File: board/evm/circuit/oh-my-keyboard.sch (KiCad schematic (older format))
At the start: 0 parts

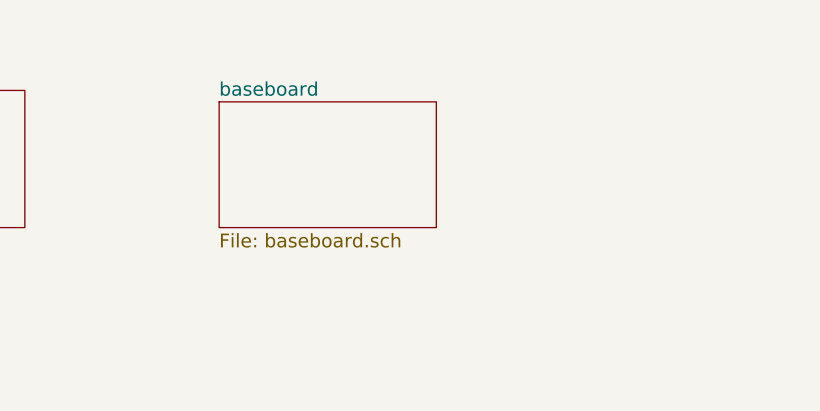
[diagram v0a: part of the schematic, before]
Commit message: add cpld
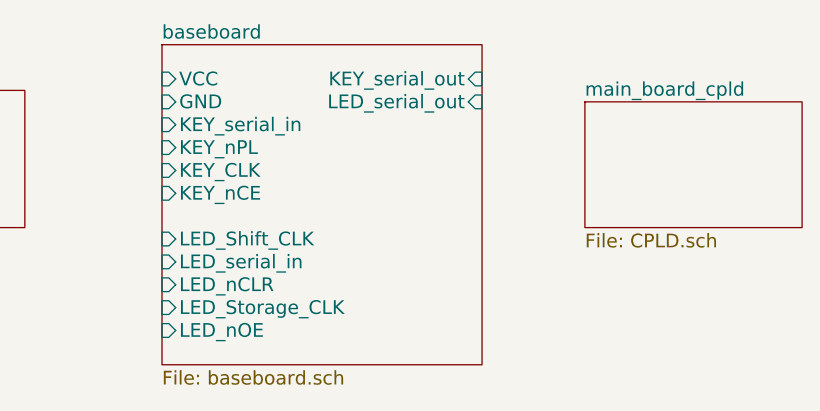
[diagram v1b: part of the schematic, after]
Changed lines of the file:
@@
 LIBS:stm8
 LIBS:stm32
+LIBS:74xgxx
+LIBS:ac-dc
+LIBS:actel
+LIBS:Altera
+LIBS:analog_devices
+LIBS:battery_management
+LIBS:bbd
+LIBS:brooktre
+LIBS:cmos_ieee
+LIBS:dc-dc
+LIBS:diode
+LIBS:elec-unifil
+LIBS:ESD_Protection
+LIBS:ftdi
+LIBS:gennum
+LIBS:graphic
+LIBS:hc11
+LIBS:ir
+LIBS:Lattice
+LIBS:logo
+LIBS:maxim
+LIBS:microchip_dspic33dsc
+LIBS:microchip_pic10mcu
+LIBS:microchip_pic12mcu
+LIBS:microchip_pic16mcu
+LIBS:microchip_pic18mcu
+LIBS:microchip_pic32mcu
+LIBS:motor_drivers
+LIBS:msp430
+LIBS:nordicsemi
+LIBS:nxp_armmcu
+LIBS:onsemi
+LIBS:Oscillators
+LIBS:powerint
+LIBS:Power_Management
+LIBS:pspice
+LIBS:references
+LIBS:relays
+LIBS:rfcom
+LIBS:sensors
+LIBS:silabs
+LIBS:supertex
+LIBS:switches
+LIBS:transf
+LIBS:ttl_ieee
+LIBS:video
+LIBS:Worldsemi
+LIBS:Xicor
+LIBS:Zilog
+LIBS:my_kicad
 LIBS:oh-my-keyboard-cache
 EELAYER 25 0
@@
 $Descr A2 23386 16535
 encoding utf-8
-Sheet 1 3
+Sheet 1 4
 Title ""
 Date ""
@@
 $EndSheet
 $Sheet
-S 3800 1700 950  550
+S 3550 1450 1400 1400
 U 57532E7E
 F0 "baseboard" 60
 F1 "baseboard.sch" 60
+F2 "VCC" I L 3550 1600 60
+F3 "GND" I L 3550 1700 60
+F4 "KEY_serial_in" I L 3550 1800 60
+F5 "KEY_nPL" I L 3550 1900 60
+F6 "KEY_CLK" I L 3550 2000 60
+F7 "KEY_nCE" I L 3550 2100 60
+F8 "KEY_serial_out" I R 4950 1600 60
+F9 "LED_Shift_CLK" I L 3550 2300 60
+F10 "LED_serial_in" I L 3550 2400 60
+F11 "LED_nCLR" I L 3550 2500 60
+F12 "LED_Storage_CLK" I L 3550 2600 60
+F13 "LED_nOE" I L 3550 2700 60
+F14 "LED_serial_out" I R 4950 1700 60
+$EndSheet
+$Sheet
+S 5400 1700 950  550
+U 5755DB2C
+F0 "main_board_cpld" 60
+F1 "CPLD.sch" 60
 $EndSheet
 $EndSCHEMATC

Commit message: add lots of ICs
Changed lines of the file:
@@
 $Descr A2 23386 16535
 encoding utf-8
-Sheet 1 4
+Sheet 1 8
 Title ""
 Date ""
@@
 F1 "CPLD.sch" 60
 $EndSheet
+$Sheet
+S 2100 3300 1400 950
+U 57545D59
+F0 "nRF24L01" 60
+F1 "nrf24l01.sch" 60
+$EndSheet
+$Sheet
+S 4100 3300 2050 1000
+U 57545D83
+F0 "BlueTooth" 60
+F1 "bluetooth.sch" 60
+$EndSheet
+$Sheet
+S 2150 4750 1400 900
+U 5754760F
+F0 "UsbDongle" 60
+F1 "usb_dongle.sch" 60
+$EndSheet
+$Sheet
+S 4150 4750 1700 850
+U 57549417
+F0 "Touch" 60
+F1 "touch.sch" 60
+$EndSheet
 $EndSCHEMATC

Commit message: basic works for mcu
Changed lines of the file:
@@
 LIBS:contrib
 LIBS:valves
-LIBS:stm8
-LIBS:stm32
-LIBS:74xgxx
-LIBS:ac-dc
-LIBS:actel
 LIBS:Altera
-LIBS:analog_devices
-LIBS:battery_management
-LIBS:bbd
-LIBS:brooktre
-LIBS:cmos_ieee
-LIBS:dc-dc
-LIBS:diode
-LIBS:elec-unifil
-LIBS:ESD_Protection
-LIBS:ftdi
-LIBS:gennum
-LIBS:graphic
-LIBS:hc11
-LIBS:ir
-LIBS:Lattice
-LIBS:logo
-LIBS:maxim
-LIBS:microchip_dspic33dsc
-LIBS:microchip_pic10mcu
-LIBS:microchip_pic12mcu
-LIBS:microchip_pic16mcu
-LIBS:microchip_pic18mcu
-LIBS:microchip_pic32mcu
-LIBS:motor_drivers
-LIBS:msp430
-LIBS:nordicsemi
-LIBS:nxp_armmcu
-LIBS:onsemi
-LIBS:Oscillators
-LIBS:powerint
-LIBS:Power_Management
-LIBS:pspice
-LIBS:references
-LIBS:relays
-LIBS:rfcom
-LIBS:sensors
-LIBS:silabs
-LIBS:supertex
-LIBS:switches
-LIBS:transf
-LIBS:ttl_ieee
-LIBS:video
-LIBS:Worldsemi
-LIBS:Xicor
-LIBS:Zilog
 LIBS:my_kicad
 LIBS:oh-my-keyboard-cache
@@
 F0 "MCU" 60
 F1 "mcu.sch" 60
+F2 "VCC" I L 2050 1750 60
+F3 "GND" I L 2050 1900 60
+F4 "VCC_5V" I L 2050 2050 60
 $EndSheet
 $Sheet

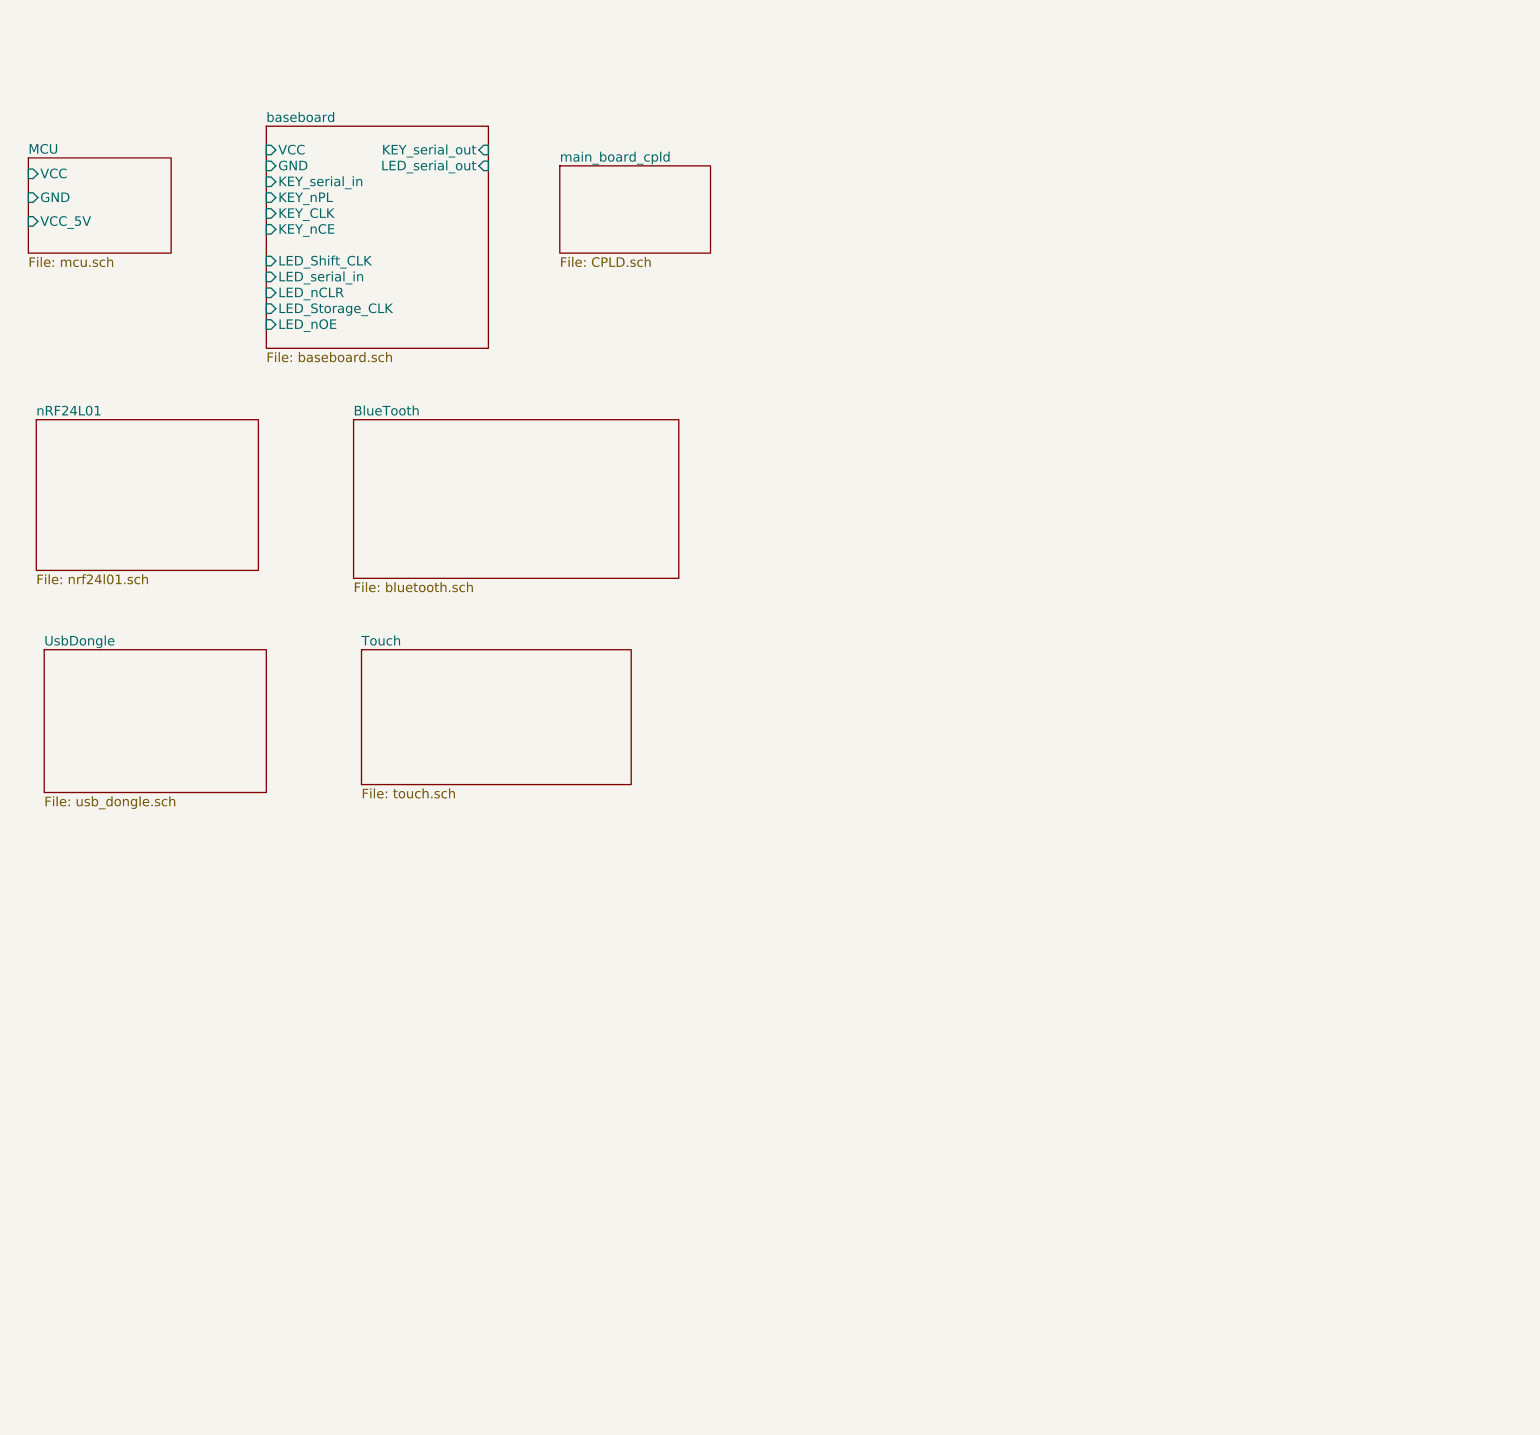
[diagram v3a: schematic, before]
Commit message: add more schs
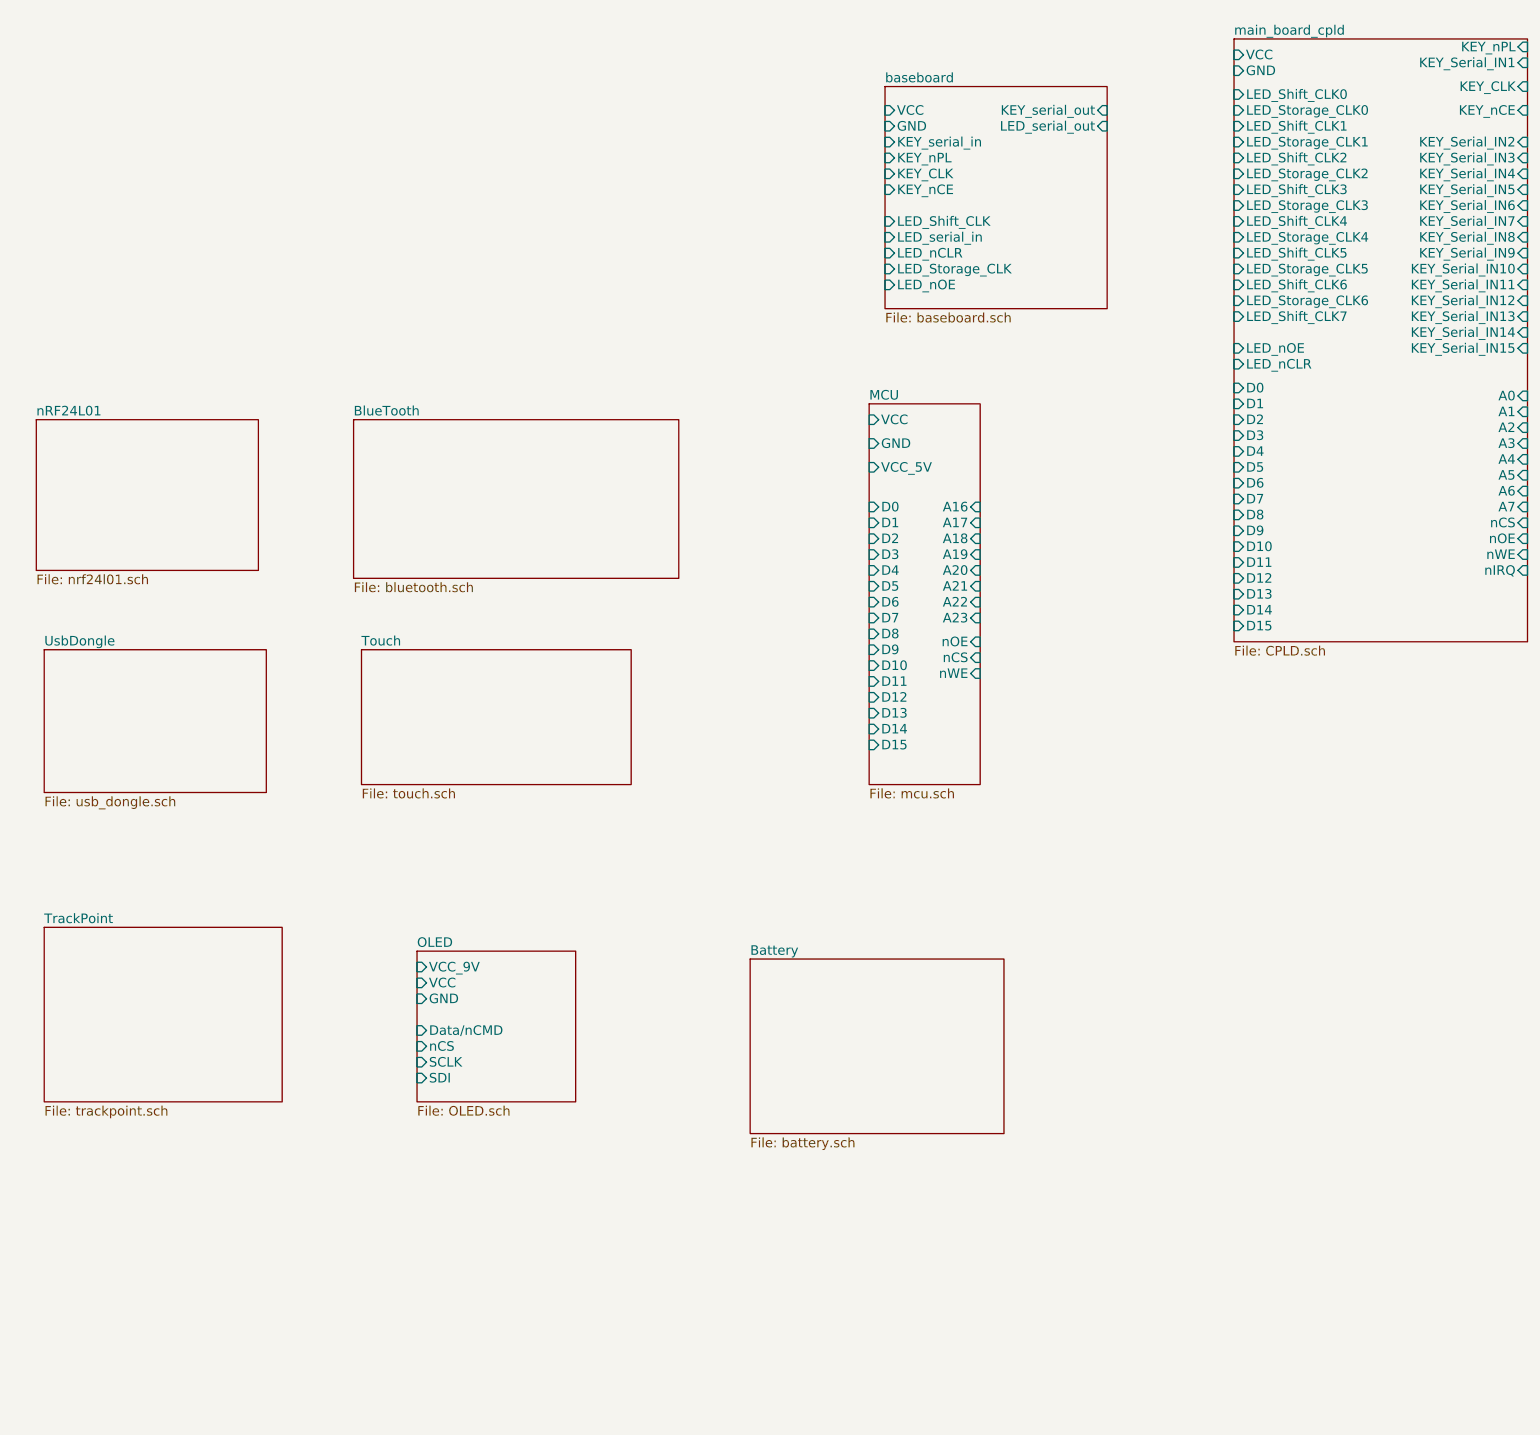
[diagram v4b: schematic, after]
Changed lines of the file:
@@
 LIBS:contrib
 LIBS:valves
+LIBS:stm8
+LIBS:stm32
+LIBS:74xgxx
+LIBS:ac-dc
+LIBS:actel
 LIBS:Altera
+LIBS:analog_devices
+LIBS:battery_management
+LIBS:bbd
+LIBS:brooktre
+LIBS:cmos_ieee
+LIBS:dc-dc
+LIBS:diode
+LIBS:elec-unifil
+LIBS:ESD_Protection
+LIBS:ftdi
+LIBS:gennum
+LIBS:graphic
+LIBS:hc11
+LIBS:ir
+LIBS:Lattice
+LIBS:logo
+LIBS:maxim
+LIBS:microchip_dspic33dsc
+LIBS:microchip_pic10mcu
+LIBS:microchip_pic12mcu
+LIBS:microchip_pic16mcu
+LIBS:microchip_pic18mcu
+LIBS:microchip_pic32mcu
+LIBS:motor_drivers
+LIBS:msp430
+LIBS:nordicsemi
+LIBS:nxp_armmcu
+LIBS:onsemi
+LIBS:Oscillators
+LIBS:powerint
+LIBS:Power_Management
+LIBS:pspice
+LIBS:references
+LIBS:relays
+LIBS:rfcom
+LIBS:sensors
+LIBS:silabs
+LIBS:supertex
+LIBS:switches
+LIBS:transf
+LIBS:ttl_ieee
+LIBS:video
+LIBS:Worldsemi
+LIBS:Xicor
+LIBS:Zilog
 LIBS:my_kicad
 LIBS:oh-my-keyboard-cache
@@
 $Descr A2 23386 16535
 encoding utf-8
-Sheet 1 8
+Sheet 1 11
 Title ""
 Date ""
@@
 $EndDescr
 $Sheet
-S 2050 1650 900  600
+S 7350 3200 700  2400
 U 57532E7B
 F0 "MCU" 60
 F1 "mcu.sch" 60
-F2 "VCC" I L 2050 1750 60
-F3 "GND" I L 2050 1900 60
-F4 "VCC_5V" I L 2050 2050 60
-$EndSheet
-$Sheet
-S 3550 1450 1400 1400
+F2 "VCC" I L 7350 3300 60
+F3 "GND" I L 7350 3450 60
+F4 "VCC_5V" I L 7350 3600 60
+F5 "D0" I L 7350 3850 60
+F6 "D1" I L 7350 3950 60
+F7 "D2" I L 7350 4050 60
+F8 "D3" I L 7350 4150 60
+F9 "D4" I L 7350 4250 60
+F10 "D5" I L 7350 4350 60
+F11 "D6" I L 7350 4450 60
+F12 "D7" I L 7350 4550 60
+F13 "D8" I L 7350 4650 60
+F14 "D9" I L 7350 4750 60
+F15 "D10" I L 7350 4850 60
+F16 "D11" I L 7350 4950 60
+F17 "D12" I L 7350 5050 60
+F18 "D13" I L 7350 5150 60
+F19 "D14" I L 7350 5250 60
+F20 "D15" I L 7350 5350 60
+F21 "A16" I R 8050 3850 60
+F22 "A17" I R 8050 3950 60
+F23 "A18" I R 8050 4050 60
+F24 "A19" I R 8050 4150 60
+F25 "A20" I R 8050 4250 60
+F26 "A21" I R 8050 4350 60
+F27 "A22" I R 8050 4450 60
+F28 "A23" I R 8050 4550 60
+F29 "nOE" I R 8050 4700 60
+F30 "nCS" I R 8050 4800 60
+F31 "nWE" I R 8050 4900 60
+$EndSheet
+$Sheet
+S 7450 1200 1400 1400
 U 57532E7E
 F0 "baseboard" 60
 F1 "baseboard.sch" 60
-F2 "VCC" I L 3550 1600 60
-F3 "GND" I L 3550 1700 60
-F4 "KEY_serial_in" I L 3550 1800 60
-F5 "KEY_nPL" I L 3550 1900 60
-F6 "KEY_CLK" I L 3550 2000 60
-F7 "KEY_nCE" I L 3550 2100 60
-F8 "KEY_serial_out" I R 4950 1600 60
-F9 "LED_Shift_CLK" I L 3550 2300 60
-F10 "LED_serial_in" I L 3550 2400 60
-F11 "LED_nCLR" I L 3550 2500 60
-F12 "LED_Storage_CLK" I L 3550 2600 60
-F13 "LED_nOE" I L 3550 2700 60
-F14 "LED_serial_out" I R 4950 1700 60
-$EndSheet
-$Sheet
-S 5400 1700 950  550
+F2 "VCC" I L 7450 1350 60
+F3 "GND" I L 7450 1450 60
+F4 "KEY_serial_in" I L 7450 1550 60
+F5 "KEY_nPL" I L 7450 1650 60
+F6 "KEY_CLK" I L 7450 1750 60
+F7 "KEY_nCE" I L 7450 1850 60
+F8 "KEY_serial_out" I R 8850 1350 60
+F9 "LED_Shift_CLK" I L 7450 2050 60
+F10 "LED_serial_in" I L 7450 2150 60
+F11 "LED_nCLR" I L 7450 2250 60
+F12 "LED_Storage_CLK" I L 7450 2350 60
+F13 "LED_nOE" I L 7450 2450 60
+F14 "LED_serial_out" I R 8850 1450 60
+$EndSheet
+$Sheet
+S 9650 900  1850 3800
 U 5755DB2C
 F0 "main_board_cpld" 60
 F1 "CPLD.sch" 60
+F2 "VCC" I L 9650 1000 60
+F3 "GND" I L 9650 1100 60
+F4 "LED_Shift_CLK0" I L 9650 1250 60
+F5 "LED_Storage_CLK0" I L 9650 1350 60
+F6 "LED_nCLR" I L 9650 2950 60
+F7 "LED_nOE" I L 9650 2850 60
+F8 "KEY_Serial_IN1" I R 11500 1050 60
+F9 "KEY_nPL" I R 11500 950 60
+F10 "KEY_CLK" I R 11500 1200 60
+F11 "KEY_nCE" I R 11500 1350 60
+F12 "KEY_Serial_IN2" I R 11500 1550 60
+F13 "KEY_Serial_IN3" I R 11500 1650 60
+F14 "KEY_Serial_IN4" I R 11500 1750 60
+F15 "KEY_Serial_IN5" I R 11500 1850 60
+F16 "KEY_Serial_IN6" I R 11500 1950 60
+F17 "KEY_Serial_IN8" I R 11500 2150 60
+F18 "KEY_Serial_IN9" I R 11500 2250 60
+F19 "KEY_Serial_IN10" I R 11500 2350 60
+F20 "KEY_Serial_IN11" I R 11500 2450 60
+F21 "KEY_Serial_IN12" I R 11500 2550 60
+F22 "KEY_Serial_IN13" I R 11500 2650 60
+F23 "KEY_Serial_IN14" I R 11500 2750 60
+F24 "KEY_Serial_IN15" I R 11500 2850 60
+F25 "LED_Storage_CLK1" I L 9650 1550 60
+F26 "LED_Storage_CLK2" I L 9650 1750 60
+F27 "LED_Storage_CLK3" I L 9650 1950 60
+F28 "LED_Storage_CLK4" I L 9650 2150 60
+F29 "LED_Shift_CLK1" I L 9650 1450 60
+F30 "LED_Shift_CLK2" I L 9650 1650 60
+F31 "LED_Shift_CLK3" I L 9650 1850 60
+F32 "LED_Shift_CLK4" I L 9650 2050 60
+F33 "LED_Shift_CLK5" I L 9650 2250 60
+F34 "LED_Storage_CLK5" I L 9650 2350 60
+F35 "LED_Shift_CLK6" I L 9650 2450 60
+F36 "LED_Storage_CLK6" I L 9650 2550 60
+F37 "LED_Shift_CLK7" I L 9650 2650 60
+F38 "KEY_Serial_IN7" I R 11500 2050 60
+F39 "D0" I L 9650 3100 60
+F40 "D1" I L 9650 3200 60
+F41 "D2" I L 9650 3300 60
+F42 "D3" I L 9650 3400 60
+F43 "D4" I L 9650 3500 60
+F44 "D5" I L 9650 3600 60
+F45 "D6" I L 9650 3700 60
+F46 "D7" I L 9650 3800 60
+F47 "D8" I L 9650 3900 60
+F48 "D9" I L 9650 4000 60
+F49 "D10" I L 9650 4100 60
+F50 "D11" I L 9650 4200 60
+F51 "D12" I L 9650 4300 60
+F52 "D13" I L 9650 4400 60
+F53 "D14" I L 9650 4500 60
+F54 "D15" I L 9650 4600 60
+F55 "A0" I R 11500 3150 60
+F56 "A1" I R 11500 3250 60
+F57 "A2" I R 11500 3350 60
+F58 "A3" I R 11500 3450 60
+F59 "A4" I R 11500 3550 60
+F60 "A5" I R 11500 3650 60
+F61 "A6" I R 11500 3750 60
+F62 "A7" I R 11500 3850 60
+F63 "nCS" I R 11500 3950 60
+F64 "nOE" I R 11500 4050 60
+F65 "nWE" I R 11500 4150 60
+F66 "nIRQ" I R 11500 4250 60
 $EndSheet
 $Sheet
@@
 F1 "touch.sch" 60
 $EndSheet
+$Sheet
+S 2150 6500 1500 1100
+U 57593E70
+F0 "TrackPoint" 60
+F1 "trackpoint.sch" 60
+$EndSheet
+$Sheet
+S 4500 6650 1000 950
+U 57593FB7
+F0 "OLED" 60
+F1 "OLED.sch" 60
+F2 "VCC_9V" I L 4500 6750 60
+F3 "GND" I L 4500 6950 60
+F4 "VCC" I L 4500 6850 60
+F5 "Data/nCMD" I L 4500 7150 60
+F6 "nCS" I L 4500 7250 60
+F7 "SCLK" I L 4500 7350 60
+F8 "SDI" I L 4500 7450 60
+$EndSheet
+$Sheet
+S 6600 6700 1600 1100
+U 57594611
+F0 "Battery" 60
+F1 "battery.sch" 60
+$EndSheet
 $EndSCHEMATC
